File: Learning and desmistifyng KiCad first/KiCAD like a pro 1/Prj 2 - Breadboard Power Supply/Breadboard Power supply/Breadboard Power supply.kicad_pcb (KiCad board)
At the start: 2 copper layers, 17 parts, among them J1 Barrel_Jack_Switch, J2 Screw_Terminal_01x02, J3 Conn_01x03_Pin, J4 Conn_01x02_Pin, J5 Screw_Terminal_01x02, J7 Conn_01x03_Pin, J9 Conn_01x02_Pin, SW1 SW_SPDT, U1 LM317L_SOT-89, U2 LM7805_TO220

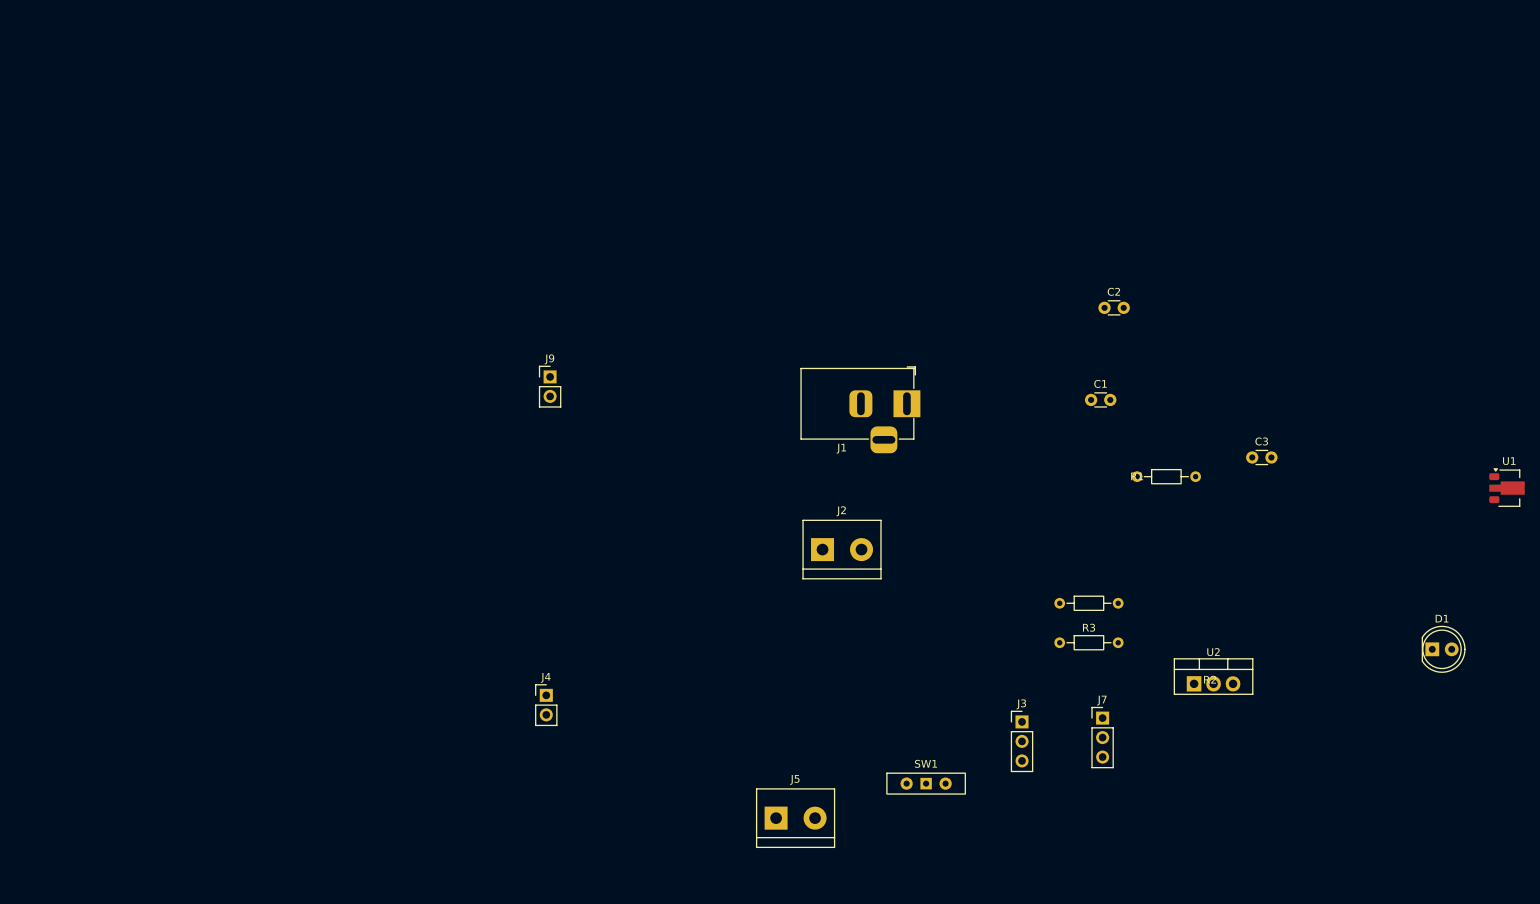
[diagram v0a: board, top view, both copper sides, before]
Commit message: update breadboard power supply project
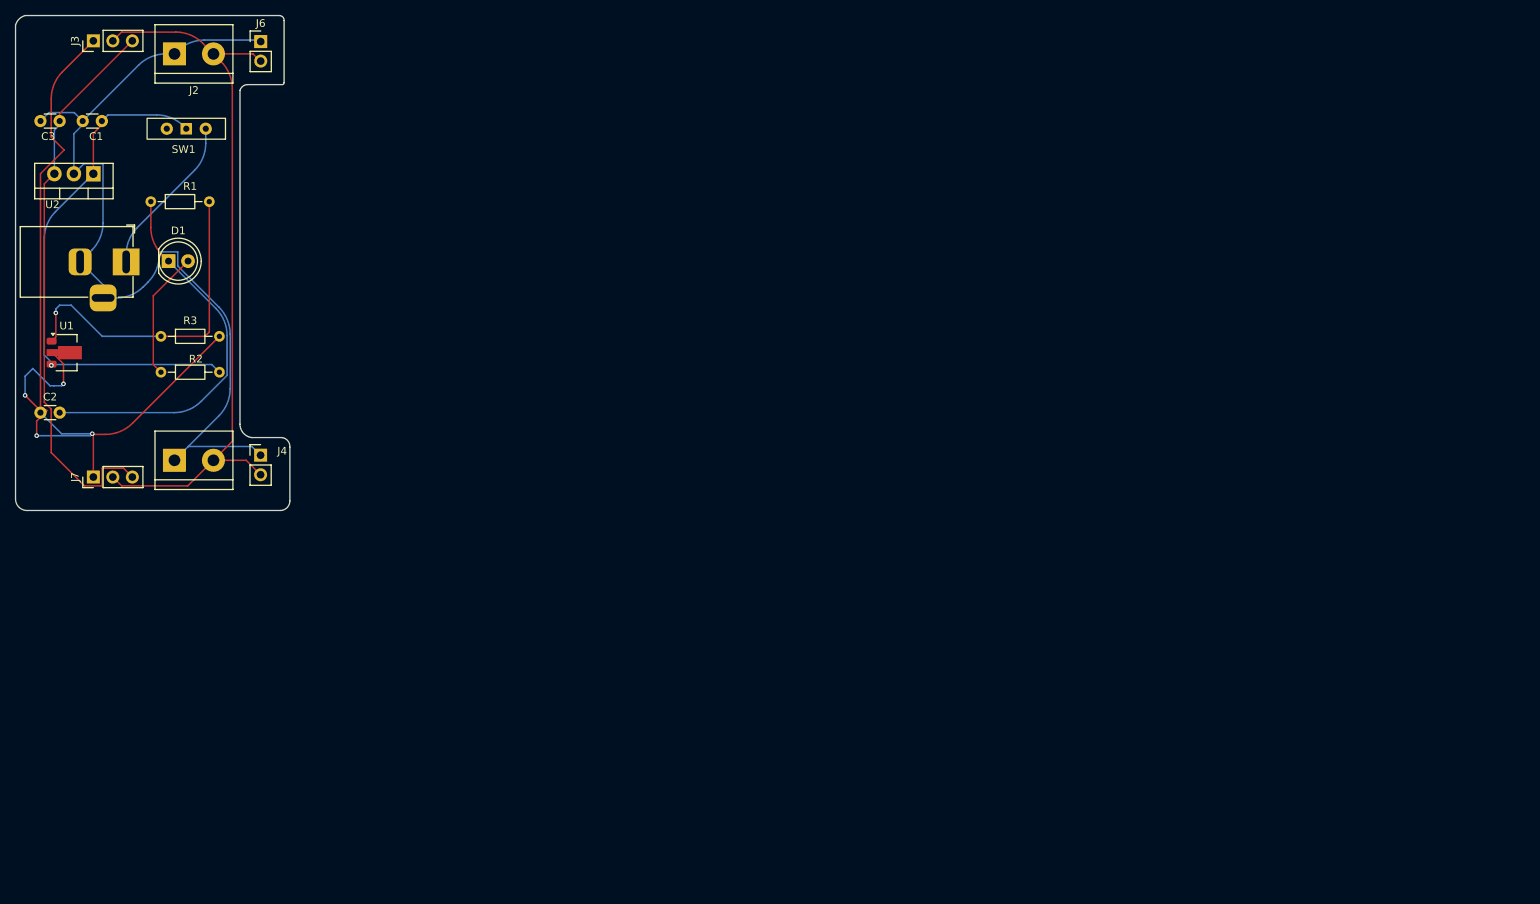
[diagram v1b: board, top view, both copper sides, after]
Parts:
- J4: value Conn_01x02_Pin -> Conn_01x02_Male
- J6: renamed from J9; value Conn_01x02_Pin -> Conn_01x02_Male
- moved U1 188.8 mm to (21.5, 69.3)
- moved D1 172.3 mm to (34.8, 57.4)
- moved C3 161.5 mm to (20.6, 39.2), turned to 180 degrees
- moved U2 158.1 mm to (25.0, 46.0), turned to 180 degrees
- moved J3 150.1 mm to (25.0, 28.7), turned to 90 degrees
- moved C2 139.3 mm to (18.1, 77.2)
- moved J7 135.2 mm to (25.0, 85.6), turned to 90 degrees
- moved C1 133.9 mm to (26.1, 39.2), turned to 180 degrees
- moved R1 133.4 mm to (32.5, 49.7)
- moved SW1 128.8 mm to (37.1, 40.2), turned to 180 degrees
- moved R3 123.7 mm to (33.8, 67.2)
- moved R2 120.9 mm to (33.8, 71.9)
- moved J2 106.3 mm to (35.5, 30.4)
- moved J1 103.4 mm to (29.2, 57.5)
- moved J5 91.2 mm to (35.5, 83.4)
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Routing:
- net GND: track 0.00 -> 120.7 mm
- net /3.3v: track 0.00 -> 116.8 mm, vias 0 -> 4
- net /PWR_output: track 0.00 -> 97.9 mm
- net /5v: track 0.00 -> 73.9 mm
- net /12v: track 0.00 -> 69.3 mm, vias 0 -> 1
- net Net-(D1-K): track 0.00 -> 49.9 mm
- net Net-(U1-ADJ): track 0.00 -> 43.5 mm, vias 0 -> 1
- net /PWR_input: track 0.00 -> 21.2 mm
- net Net-(D1-A): track 0.00 -> 16.8 mm
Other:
- board outline added: 35.8 x 64.5 mm

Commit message: update the breadboard power supply files
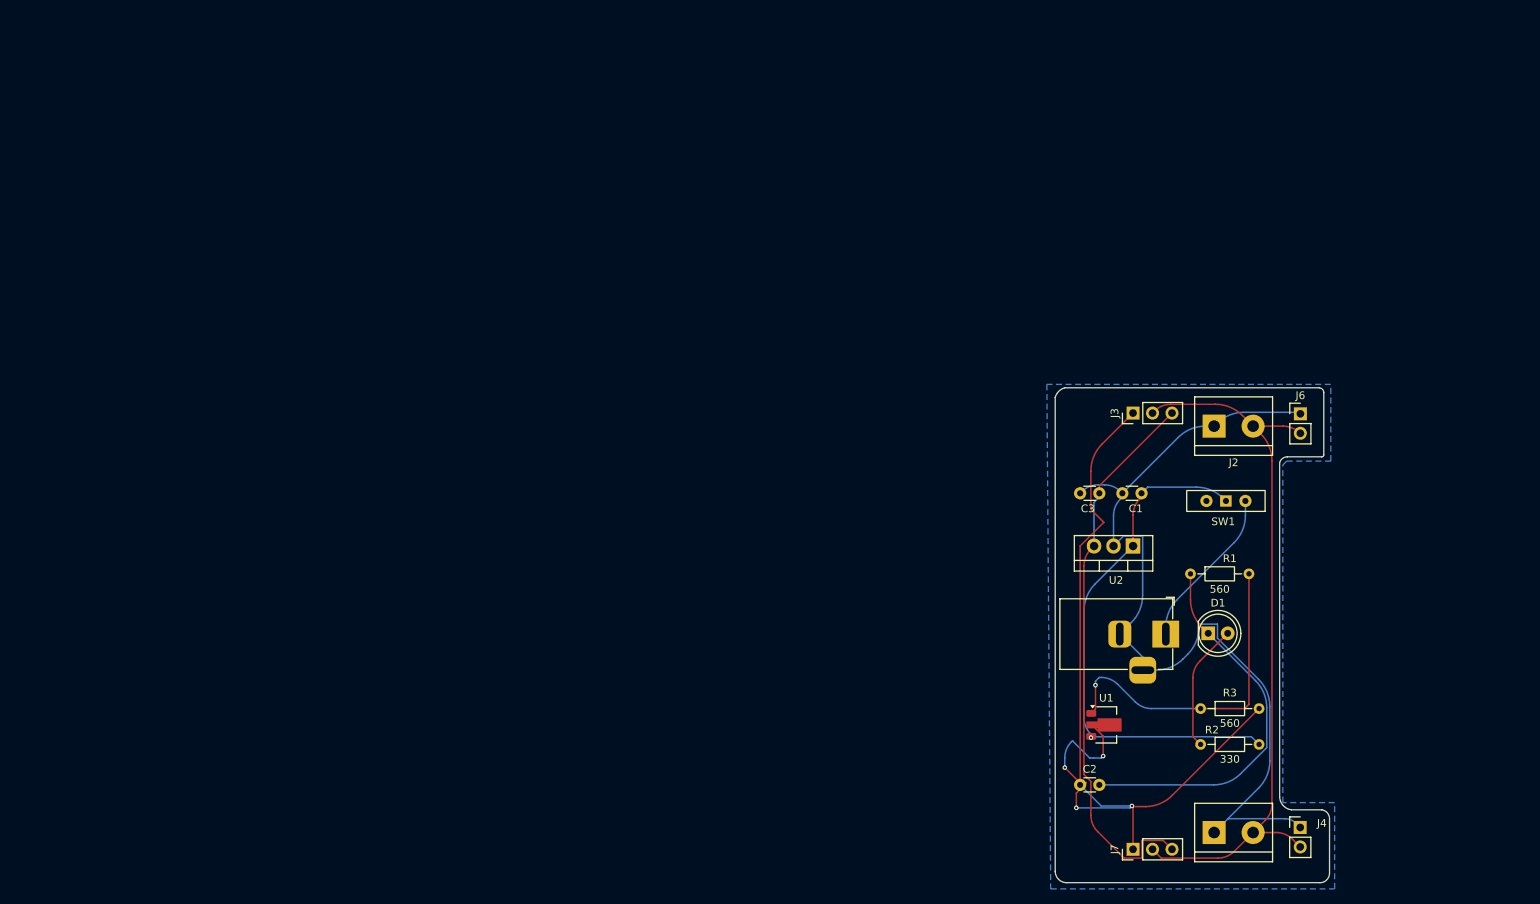
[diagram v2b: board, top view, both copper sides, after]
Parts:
- J3, J7: value Conn_01x03_Pin -> Conn_01x03_Male
- moved J1 143.9 mm to (164.7, 106.0)
- moved J2 143.9 mm to (171.0, 78.9)
- moved J4 143.9 mm to (182.3, 131.2)
- moved J5 143.9 mm to (171.0, 131.9)
- moved J6 143.9 mm to (182.3, 77.3)
- moved R2 143.9 mm to (169.3, 120.4)
- moved R3 143.9 mm to (169.3, 115.7)
- moved U1 143.9 mm to (157.0, 117.8)
- moved C1 143.9 mm to (161.6, 87.7)
- moved C2 143.9 mm to (153.6, 125.7)
- moved C3 143.9 mm to (156.1, 87.7)
- moved D1 143.9 mm to (170.3, 105.9)
- moved J3 143.9 mm to (160.5, 77.2)
- moved J7 143.9 mm to (160.5, 134.1)
- moved R1 143.9 mm to (168.0, 98.2)
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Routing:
- net /PWR_output: track 97.9 -> 97.2 mm
- net GND: track 120.7 -> 120.2 mm
- added copper zone on B.Cu, net GND
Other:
- outline, holes or cut-outs redrawn
- board text added: "Breadboard power supply"
- board text added: "v0.2"

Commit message: updates on demistifying kicad
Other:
- board text added: "v2.0"
- board text removed: "v0.2"
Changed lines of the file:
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@@
 		(layer "Edge.Cuts")
 	)
-	(gr_text "v0.2"
+	(gr_text "v2.0"
 		(at 176.75 91.75 90)
 		(layer "B.SilkS")

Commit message: update breadboard power  supply project as v1.0
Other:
- board text added: "v1.0"
- board text removed: "v2.0"
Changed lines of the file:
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@@
 		(layer "Edge.Cuts")
 	)
-	(gr_text "v2.0"
+	(gr_text "v1.0"
 		(at 176.75 91.75 90)
 		(layer "B.SilkS")
